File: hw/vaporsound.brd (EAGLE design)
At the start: 100 x 80 mm, 76 parts, among them Q1 BSS138, Q2 BSS138

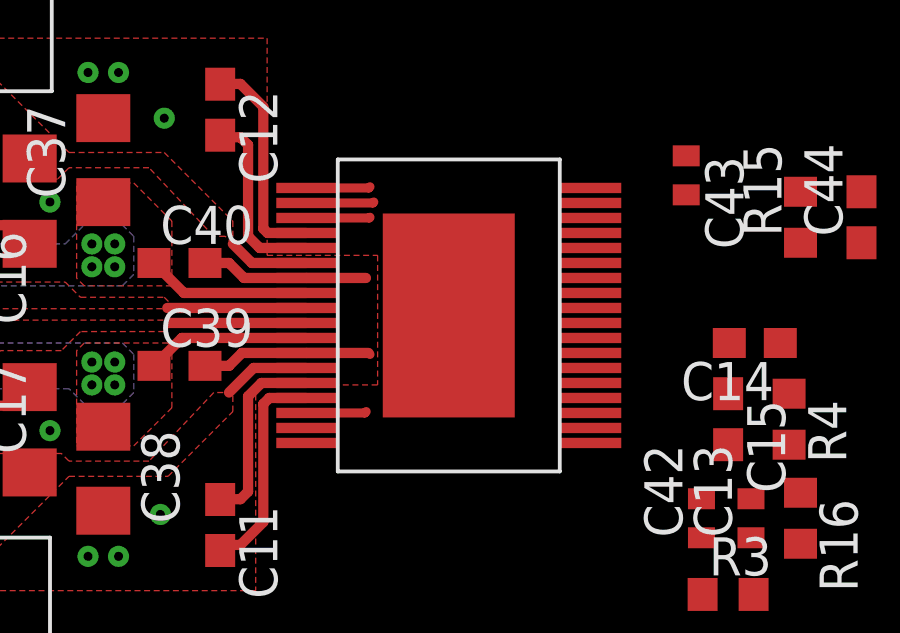
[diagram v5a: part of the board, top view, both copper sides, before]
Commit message: add thermal vias for sta350
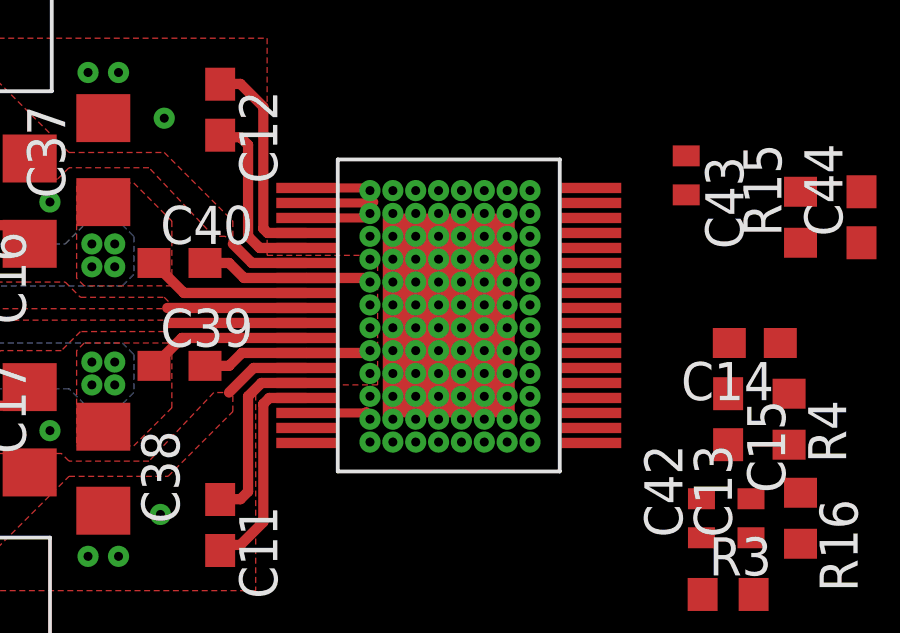
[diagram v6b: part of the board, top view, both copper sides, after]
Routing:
- net GND: vias 56 -> 152
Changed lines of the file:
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@@
 <hole x="88" y="3" drill="3.2"/>
 <hole x="88" y="77" drill="3.2"/>
-<rectangle x1="47.117" y1="42.672" x2="47.244" y2="43.053" layer="41"/>
 </plain>
 <attributes>
@@
 <via x="33.909" y="36.957" extent="1-16" drill="0.3"/>
 <contactref element="R16" pad="2"/>
+<via x="43.18" y="43.942" extent="1-16" drill="0.3"/>
+<via x="43.18" y="43.18" extent="1-16" drill="0.3"/>
+<via x="43.942" y="43.942" extent="1-16" drill="0.3"/>
+<via x="43.942" y="43.18" extent="1-16" drill="0.3"/>
+<via x="44.704" y="43.942" extent="1-16" drill="0.3"/>
+<via x="45.466" y="43.942" extent="1-16" drill="0.3"/>
+<via x="46.228" y="43.942" extent="1-16" drill="0.3"/>
+<via x="42.418" y="43.942" extent="1-16" drill="0.3"/>
+<via x="41.656" y="43.942" extent="1-16" drill="0.3"/>
+<via x="40.894" y="43.942" extent="1-16" drill="0.3"/>
+<via x="40.894" y="44.704" extent="1-16" drill="0.3"/>
+<via x="40.894" y="45.466" extent="1-16" drill="0.3"/>
+<via x="40.894" y="46.228" extent="1-16" drill="0.3"/>
+<via x="40.894" y="46.99" extent="1-16" drill="0.3"/>
+<via x="40.894" y="47.752" extent="1-16" drill="0.3"/>
+<via x="41.656" y="47.752" extent="1-16" drill="0.3"/>
+<via x="42.418" y="47.752" extent="1-16" drill="0.3"/>
+<via x="40.894" y="43.18" extent="1-16" drill="0.3"/>
+<via x="40.894" y="42.418" extent="1-16" drill="0.3"/>
+<via x="40.894" y="41.656" extent="1-16" drill="0.3"/>
+<via x="40.894" y="40.894" extent="1-16" drill="0.3"/>
+<via x="40.894" y="40.132" extent="1-16" drill="0.3"/>
+<via x="40.894" y="39.37" extent="1-16" drill="0.3"/>
+<via x="41.656" y="39.37" extent="1-16" drill="0.3"/>
+<via x="42.418" y="39.37" extent="1-16" drill="0.3"/>
+<via x="43.18" y="39.37" extent="1-16" drill="0.3"/>
+<via x="43.942" y="39.37" extent="1-16" drill="0.3"/>
+<via x="44.704" y="39.37" extent="1-16" drill="0.3"/>
+<via x="45.466" y="39.37" extent="1-16" drill="0.3"/>
+<via x="46.228" y="39.37" extent="1-16" drill="0.3"/>
+<via x="46.228" y="40.132" extent="1-16" drill="0.3"/>
+<via x="46.228" y="40.894" extent="1-16" drill="0.3"/>
+<via x="46.228" y="41.656" extent="1-16" drill="0.3"/>
+<via x="46.228" y="42.418" extent="1-16" drill="0.3"/>
+<via x="46.228" y="43.18" extent="1-16" drill="0.3"/>
+<via x="41.656" y="43.18" extent="1-16" drill="0.3"/>
+<via x="42.418" y="43.18" extent="1-16" drill="0.3"/>
+<via x="44.704" y="43.18" extent="1-16" drill="0.3"/>
+<via x="45.466" y="43.18" extent="1-16" drill="0.3"/>
+<via x="43.18" y="47.752" extent="1-16" drill="0.3"/>
+<via x="43.942" y="47.752" extent="1-16" drill="0.3"/>
+<via x="44.704" y="47.752" extent="1-16" drill="0.3"/>
+<via x="45.466" y="47.752" extent="1-16" drill="0.3"/>
+<via x="46.228" y="47.752" extent="1-16" drill="0.3"/>
+<via x="46.228" y="46.99" extent="1-16" drill="0.3"/>
+<via x="46.228" y="46.228" extent="1-16" drill="0.3"/>
+<via x="46.228" y="45.466" extent="1-16" drill="0.3"/>
+<via x="46.228" y="44.704" extent="1-16" drill="0.3"/>
+<via x="45.466" y="44.704" extent="1-16" drill="0.3"/>
+<via x="45.466" y="45.466" extent="1-16" drill="0.3"/>
+<via x="45.466" y="46.228" extent="1-16" drill="0.3"/>
+<via x="45.466" y="46.99" extent="1-16" drill="0.3"/>
+<via x="44.704" y="46.99" extent="1-16" drill="0.3"/>
+<via x="43.942" y="46.99" extent="1-16" drill="0.3"/>
+<via x="43.18" y="46.99" extent="1-16" drill="0.3"/>
+<via x="42.418" y="46.99" extent="1-16" drill="0.3"/>
+<via x="41.656" y="46.99" extent="1-16" drill="0.3"/>
+<via x="41.656" y="46.228" extent="1-16" drill="0.3"/>
+<via x="42.418" y="46.228" extent="1-16" drill="0.3"/>
+<via x="43.18" y="46.228" extent="1-16" drill="0.3"/>
+<via x="43.942" y="46.228" extent="1-16" drill="0.3"/>
+<via x="44.704" y="46.228" extent="1-16" drill="0.3"/>
+<via x="41.656" y="45.466" extent="1-16" drill="0.3"/>
+<via x="41.656" y="44.704" extent="1-16" drill="0.3"/>
+<via x="41.656" y="42.418" extent="1-16" drill="0.3"/>
+<via x="41.656" y="41.656" extent="1-16" drill="0.3"/>
+<via x="41.656" y="40.894" extent="1-16" drill="0.3"/>
+<via x="41.656" y="40.132" extent="1-16" drill="0.3"/>
+<via x="42.418" y="40.132" extent="1-16" drill="0.3"/>
+<via x="43.18" y="40.132" extent="1-16" drill="0.3"/>
+<via x="43.942" y="40.132" extent="1-16" drill="0.3"/>
+<via x="44.704" y="40.132" extent="1-16" drill="0.3"/>
+<via x="45.466" y="40.132" extent="1-16" drill="0.3"/>
+<via x="45.466" y="40.894" extent="1-16" drill="0.3"/>
+<via x="45.466" y="41.656" extent="1-16" drill="0.3"/>
+<via x="45.466" y="42.418" extent="1-16" drill="0.3"/>
+<via x="42.418" y="44.704" extent="1-16" drill="0.3"/>
+<via x="43.18" y="44.704" extent="1-16" drill="0.3"/>
+<via x="43.942" y="44.704" extent="1-16" drill="0.3"/>
+<via x="44.704" y="44.704" extent="1-16" drill="0.3"/>
+<via x="44.704" y="45.466" extent="1-16" drill="0.3"/>
+<via x="43.942" y="45.466" extent="1-16" drill="0.3"/>
+<via x="43.18" y="45.466" extent="1-16" drill="0.3"/>
+<via x="42.418" y="45.466" extent="1-16" drill="0.3"/>
+<via x="42.418" y="42.418" extent="1-16" drill="0.3"/>
+<via x="43.18" y="42.418" extent="1-16" drill="0.3"/>
+<via x="43.942" y="42.418" extent="1-16" drill="0.3"/>
+<via x="44.704" y="42.418" extent="1-16" drill="0.3"/>
+<via x="44.704" y="41.656" extent="1-16" drill="0.3"/>
+<via x="44.704" y="40.894" extent="1-16" drill="0.3"/>
+<via x="42.418" y="41.656" extent="1-16" drill="0.3"/>
+<via x="42.418" y="40.894" extent="1-16" drill="0.3"/>
+<via x="43.18" y="40.894" extent="1-16" drill="0.3"/>
+<via x="43.942" y="40.894" extent="1-16" drill="0.3"/>
+<via x="43.942" y="41.656" extent="1-16" drill="0.3"/>
+<via x="43.18" y="41.656" extent="1-16" drill="0.3"/>
 </signal>
 <signal name="EPAD">

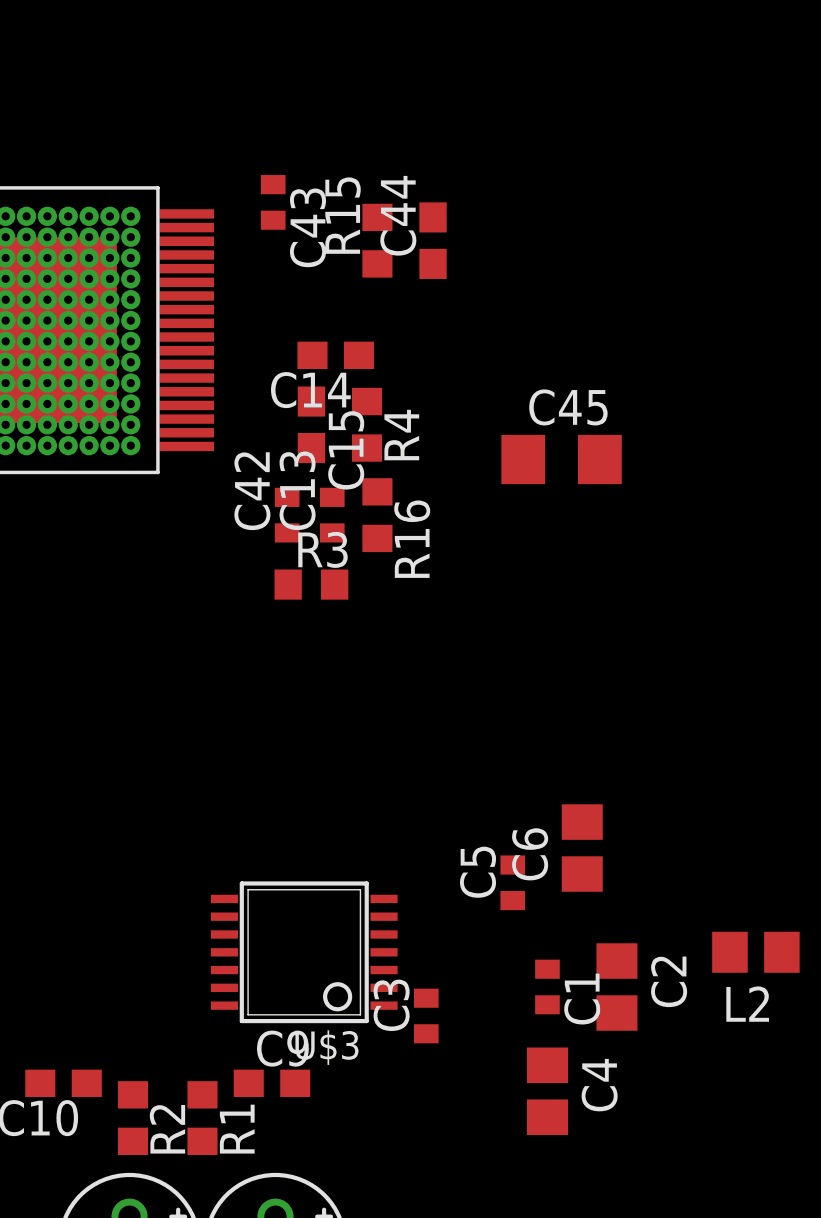
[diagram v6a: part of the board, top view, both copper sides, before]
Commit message: use 0603 capacitors instead of 0402 ones
0603 is small enough for the board
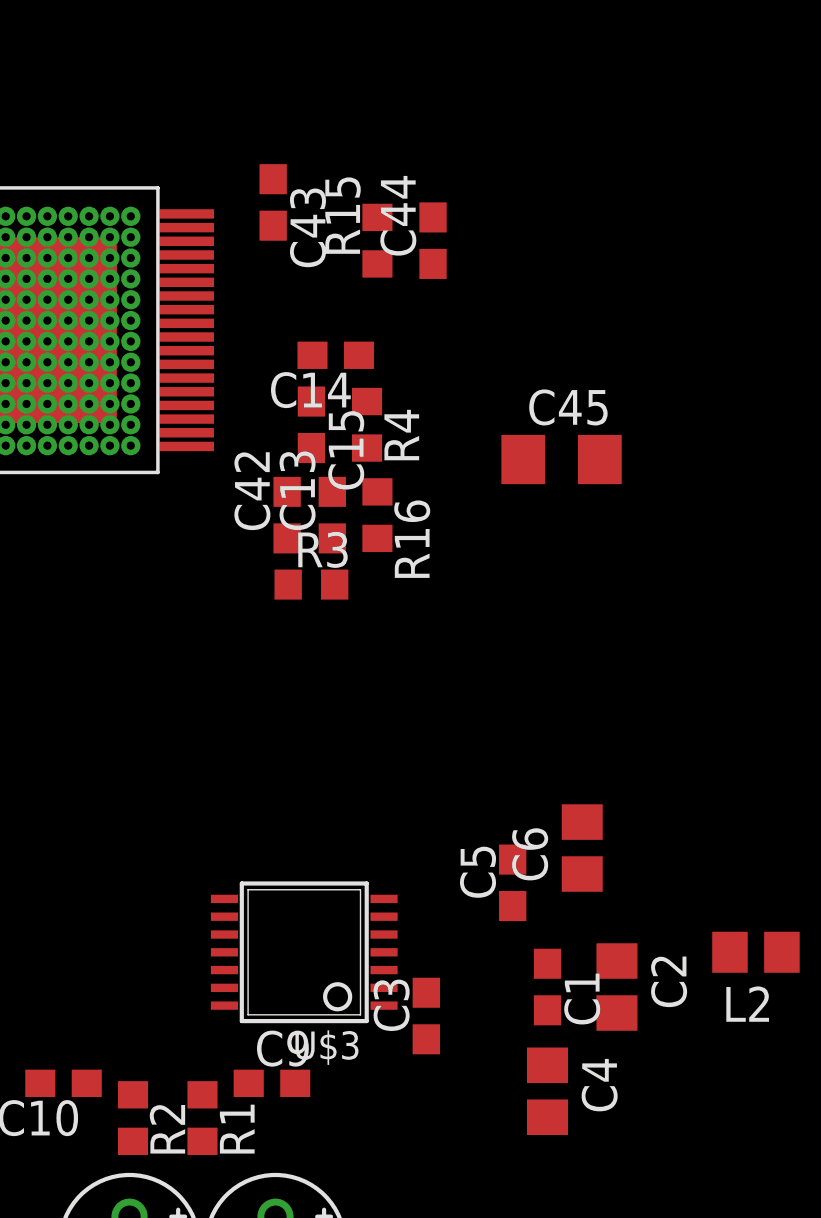
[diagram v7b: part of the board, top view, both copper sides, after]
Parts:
- C1, C13, C3, C42, C43, C5: device rcl:C0402 -> rcl:C0603
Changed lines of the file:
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@@
 <element name="U$3" library="pcm1808" package="TSSOP14" value="PCM1808" x="52.57" y="20.85" rot="R90"/>
 <element name="L2" library="rcl" package="R0805" value="" x="69.08" y="20.85" rot="R180"/>
-<element name="C1" library="rcl" package="C0402" value="100n" x="61.46" y="19.58" rot="R270"/>
+<element name="C1" library="rcl" package="C0603" value="100n" x="61.46" y="19.58" rot="R270"/>
 <element name="C2" library="rcl" package="C0805" value="" x="64" y="19.58" rot="R270"/>
-<element name="C3" library="rcl" package="C0402" value="100n" x="57.031" y="18.52" rot="R90"/>
+<element name="C3" library="rcl" package="C0603" value="100n" x="57.031" y="18.52" rot="R90"/>
 <element name="C4" library="rcl" package="C0805" value="" x="61.46" y="15.77" rot="R270"/>
-<element name="C5" library="rcl" package="C0402" value="100n" x="60.19" y="23.39" rot="R90"/>
+<element name="C5" library="rcl" package="C0603" value="100n" x="60.19" y="23.39" rot="R90"/>
 <element name="C6" library="rcl" package="C0805" value="" x="62.73" y="24.66" rot="R90"/>
 <element name="C7" library="rcl" package="E2-5" value="1u" x="51.517" y="10.17" rot="R270"/>
@@
 <element name="C12" library="rcl" package="C0603" value="100n" x="35.9" y="50.448" rot="R270"/>
 <element name="R3" library="rcl" package="R0603" value="2R2" x="52.832" y="34.29"/>
-<element name="C13" library="rcl" package="C0402" value="100n" x="53.594" y="36.83" rot="R90"/>
+<element name="C13" library="rcl" package="C0603" value="100n" x="53.594" y="36.83" rot="R90"/>
 <element name="C14" library="rcl" package="C0603" value="4n7" x="53.721" y="42.672" rot="R180"/>
 <element name="C15" library="rcl" package="C0603" value="680p" x="52.832" y="40.132" rot="R270"/>
@@
 <element name="C40" library="rcl" package="C0603" value="100n" x="34.544" y="45.339"/>
 <element name="C41" library="rcl" package="E5-10,5" value="1000u" x="17.653" y="43.561" rot="R180"/>
-<element name="C42" library="rcl" package="C0402" value="100n" x="51.943" y="36.83" rot="R90"/>
-<element name="C43" library="rcl" package="C0402" value="100n" x="51.435" y="48.26" rot="R270"/>
+<element name="C42" library="rcl" package="C0603" value="100n" x="51.943" y="36.83" rot="R90"/>
+<element name="C43" library="rcl" package="C0603" value="100n" x="51.435" y="48.26" rot="R270"/>
 <element name="R15" library="rcl" package="R0603" value="10k" x="55.245" y="46.863" rot="R90"/>
 <element name="C44" library="rcl" package="C0603" value="1n" x="57.277" y="46.863" rot="R90"/>
@@
 <contactref element="L2" pad="2"/>
 <wire x1="64" y1="20.53" x2="68.13" y2="20.85" width="0" layer="19" extent="1-1"/>
-<wire x1="61.46" y1="20.23" x2="64" y2="20.53" width="0" layer="19" extent="1-1"/>
-<wire x1="55.4878" y1="20.2" x2="61.46" y2="20.23" width="0" layer="19" extent="1-1"/>
+<wire x1="61.46" y1="20.43" x2="64" y2="20.53" width="0" layer="19" extent="1-1"/>
+<wire x1="55.4878" y1="20.2" x2="61.46" y2="20.43" width="0" layer="19" extent="1-1"/>
 </signal>
 <signal name="+5V">
@@
 <wire x1="85.85" y1="39" x2="85.85" y2="41.127" width="0" layer="19" extent="1-1"/>
 <wire x1="60.576" y1="38.862" x2="85.85" y2="39" width="0" layer="19" extent="1-1"/>
-<wire x1="51.943" y1="36.18" x2="60.576" y2="38.862" width="0" layer="19" extent="1-1"/>
-<wire x1="51.982" y1="34.29" x2="51.943" y2="36.18" width="0" layer="19" extent="1-1"/>
-<wire x1="48.27" y1="40.34" x2="51.943" y2="36.18" width="0" layer="19" extent="1-1"/>
+<wire x1="51.943" y1="35.98" x2="60.576" y2="38.862" width="0" layer="19" extent="1-1"/>
+<wire x1="51.982" y1="34.29" x2="51.943" y2="35.98" width="0" layer="19" extent="1-1"/>
+<wire x1="48.27" y1="40.34" x2="51.943" y2="35.98" width="0" layer="19" extent="1-1"/>
 <wire x1="48.27" y1="47.84" x2="48.27" y2="40.34" width="0" layer="19" extent="1-1"/>
-<wire x1="51.435" y1="48.91" x2="48.27" y2="47.84" width="0" layer="19" extent="1-1"/>
-<wire x1="55.245" y1="47.713" x2="51.435" y2="48.91" width="0" layer="19" extent="1-1"/>
+<wire x1="51.435" y1="49.11" x2="48.27" y2="47.84" width="0" layer="19" extent="1-1"/>
+<wire x1="55.245" y1="47.713" x2="51.435" y2="49.11" width="0" layer="19" extent="1-1"/>
 <wire x1="55.4878" y1="20.85" x2="51.982" y2="34.29" width="0" layer="19" extent="1-1"/>
-<wire x1="60.19" y1="22.74" x2="55.4878" y2="20.85" width="0" layer="19" extent="1-1"/>
-<wire x1="62.73" y1="23.71" x2="60.19" y2="22.74" width="0" layer="19" extent="1-1"/>
+<wire x1="60.19" y1="22.54" x2="55.4878" y2="20.85" width="0" layer="19" extent="1-1"/>
+<wire x1="62.73" y1="23.71" x2="60.19" y2="22.54" width="0" layer="19" extent="1-1"/>
 <wire x1="77.84" y1="13" x2="62.73" y2="23.71" width="0" layer="19" extent="1-1"/>
 <wire x1="81.84" y1="13" x2="77.84" y2="13" width="0" layer="19" extent="1-1"/>
@@
 <contactref element="C3" pad="1"/>
 <contactref element="C4" pad="1"/>
-<wire x1="57.031" y1="17.87" x2="61.46" y2="16.72" width="0" layer="19" extent="1-1"/>
-<wire x1="55.4878" y1="18.9" x2="57.031" y2="17.87" width="0" layer="19" extent="1-1"/>
+<wire x1="57.031" y1="17.67" x2="61.46" y2="16.72" width="0" layer="19" extent="1-1"/>
+<wire x1="55.4878" y1="18.9" x2="57.031" y2="17.67" width="0" layer="19" extent="1-1"/>
 </signal>
 <signal name="C_RIGHT">
@@
 <contactref element="U$1" pad="P$24"/>
 <contactref element="C13" pad="1"/>
-<wire x1="53.594" y1="36.18" x2="48.27" y2="41.84" width="0" layer="19" extent="1-1"/>
-<wire x1="53.682" y1="34.29" x2="53.594" y2="36.18" width="0" layer="19" extent="1-1"/>
+<wire x1="53.594" y1="35.98" x2="48.27" y2="41.84" width="0" layer="19" extent="1-1"/>
+<wire x1="53.682" y1="34.29" x2="53.594" y2="35.98" width="0" layer="19" extent="1-1"/>
 </signal>
 <signal name="FILTER_PLL">
@@
 <contactref element="C13" pad="2"/>
 <wire x1="52.832" y1="39.282" x2="52.871" y2="42.672" width="0" layer="19" extent="1-1"/>
-<wire x1="53.594" y1="37.48" x2="52.832" y2="39.282" width="0" layer="19" extent="1-1"/>
-<wire x1="55.245" y1="37.68" x2="53.594" y2="37.48" width="0" layer="19" extent="1-1"/>
+<wire x1="53.594" y1="37.68" x2="52.832" y2="39.282" width="0" layer="19" extent="1-1"/>
+<wire x1="55.245" y1="37.68" x2="53.594" y2="37.68" width="0" layer="19" extent="1-1"/>
 <wire x1="48.27" y1="42.84" x2="52.871" y2="42.672" width="0" layer="19" extent="1-1"/>
 </signal>

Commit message: do some more floorplanning
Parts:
- moved R13 51.9 mm to (75.2, 55.8), flipped to the bottom, turned to 90 degrees
- moved R14 51.8 mm to (77.7, 55.8), flipped to the bottom, turned to 90 degrees
- moved SV1 45.6 mm to (79.0, 52.5), turned to 180 degrees
- moved C10 36.7 mm to (80.4, 14.9), flipped to the bottom
- moved Q2 34.6 mm to (71.7, 45.3), flipped to the bottom, turned to 270 degrees
- moved C8 34.2 mm to (80.3, 8.90)
- moved Q1 33.3 mm to (78.9, 45.3), flipped to the bottom, turned to 270 degrees
- moved R2 33.3 mm to (79.5, 12.4), flipped to the bottom
- moved SV2 28.9 mm to (77.7, 3.76), turned to 180 degrees
- moved R1 27.9 mm to (76.6, 12.5), flipped to the bottom
- moved C9 24.6 mm to (76.0, 15.0), flipped to the bottom
- moved C7 23.5 mm to (75.0, 8.90)
- moved U$3 23.3 mm to (75.8, 20.2), flipped to the bottom
- moved C3 14.7 mm to (71.7, 16.9), flipped to the bottom, turned to 0 degrees
- moved R12 11.5 mm to (74.3, 45.3), flipped to the bottom, turned to 90 degrees
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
